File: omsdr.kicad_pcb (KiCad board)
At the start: 2 copper layers, 50 x 50 mm, 57 parts, among them J1 I/Q Out, J2 ANT, J3 ISP, J4 LO, J5 I/Q Out, J8 PWR, SW1 SW_SPST, SW2 SW_SPST, T1 CX2074NL, U1 LT6231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

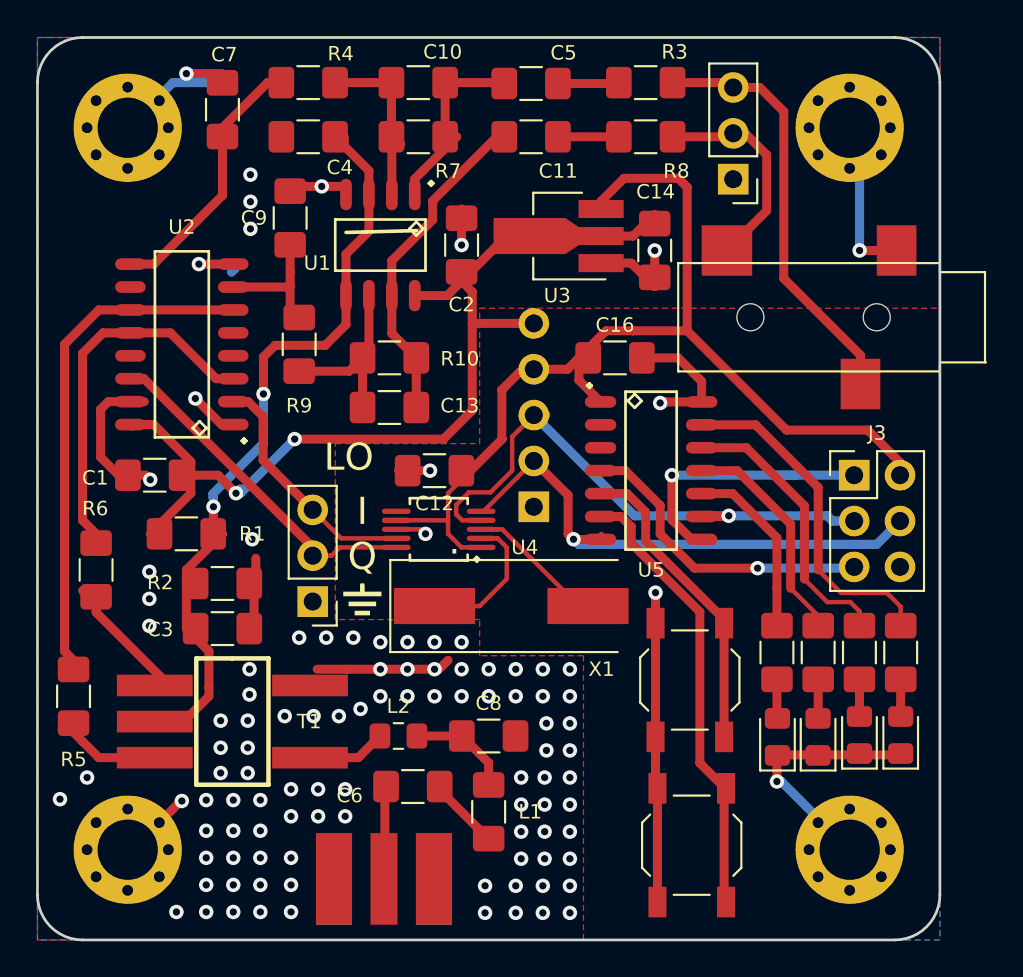
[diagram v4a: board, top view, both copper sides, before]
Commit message: Replaced connector footprints with versions from new kicad footprint library
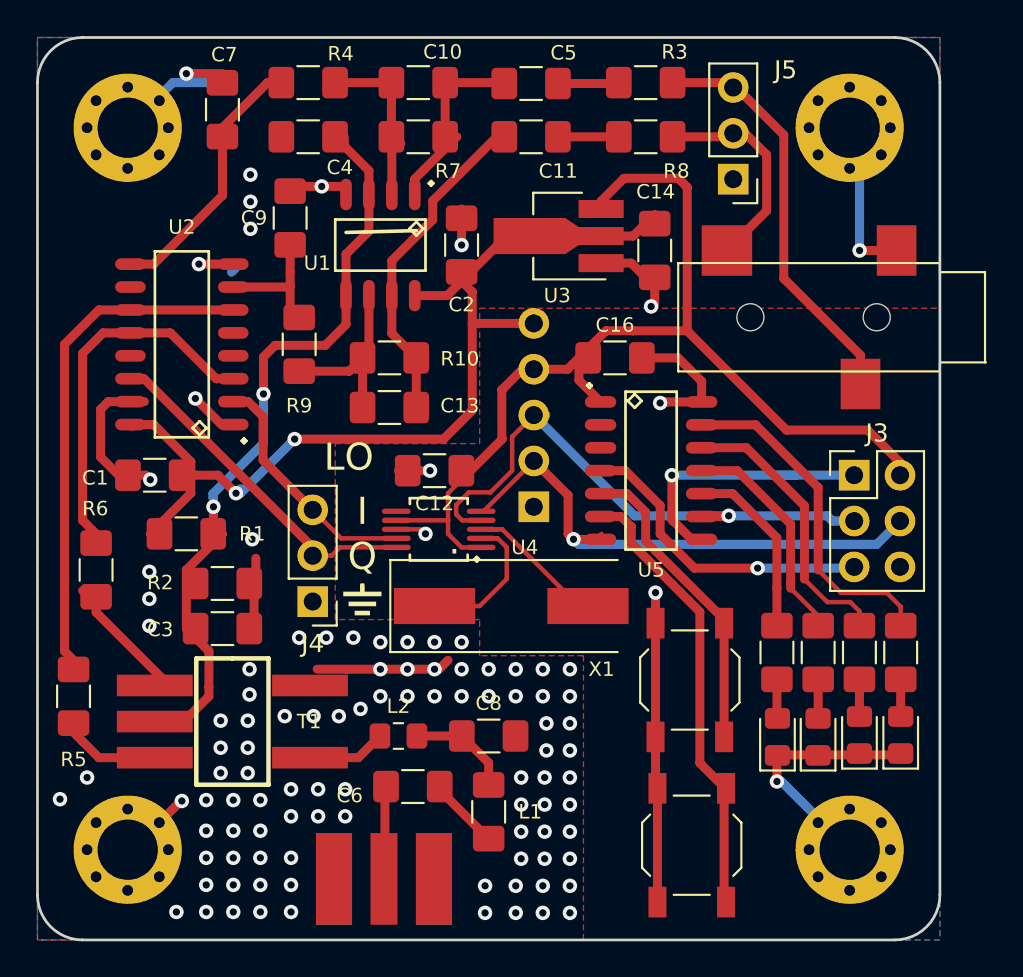
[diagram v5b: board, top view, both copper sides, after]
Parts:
- J3: footprint Pin_Headers:Pin_Header_Straight_2x03_Pitch2.54mm -> Connector_PinHeader_2.54mm:PinHeader_2x03_P2.54mm_Vertical
- J4: footprint Pin_Headers:Pin_Header_Straight_1x03_Pitch2.54mm -> Connector_PinHeader_2.54mm:PinHeader_1x03_P2.54mm_Vertical
- J8: footprint Pin_Headers:Pin_Header_Angled_1x05_Pitch2.54mm -> Connector_PinHeader_2.54mm:PinHeader_1x05_P2.54mm_Horizontal
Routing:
- net Net-(J1-Pad2): track 24.2 -> 23.4 mm

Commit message: Bumping version to 1.2 on schematic and PCB
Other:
- board text added: "OMSDR Rev. 1.2"
- board text removed: "OMSDR Rev. 1.1"
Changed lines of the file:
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@@
     (effects (font (size 1 1) (thickness 0.2)) (justify left mirror))
   )
-  (gr_text "OMSDR Rev. 1.1" (at 147.5 81.75) (layer B.SilkS)
+  (gr_text "OMSDR Rev. 1.2" (at 147.5 81.75) (layer B.SilkS)
     (effects (font (size 1.5 1.5) (thickness 0.3)) (justify left mirror))
   )

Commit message: Now official HB9UF project, add logo and rework silk.
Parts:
- added G***: LOGO, local:hb9uf_logo_small, B.Cu at (126.0, 88.0)
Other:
- board text added: "Based on work by T. Parks (c) 2017,18,19 CC-BY-SA"
- board text added: "HB9UF OMSDR"
- board text added: "by Matt Weyland HB9FRV, Rev. 1.2"
- board text removed: "Based on work by Tony Parks (c) 2017,18,19 CC-BY-SA"
- board text removed: "OMSDR Rev. 1.2"
- board text removed: "by Matt Weyland (HB9FRV) and Peter Klaentschi (HB9GHY)"

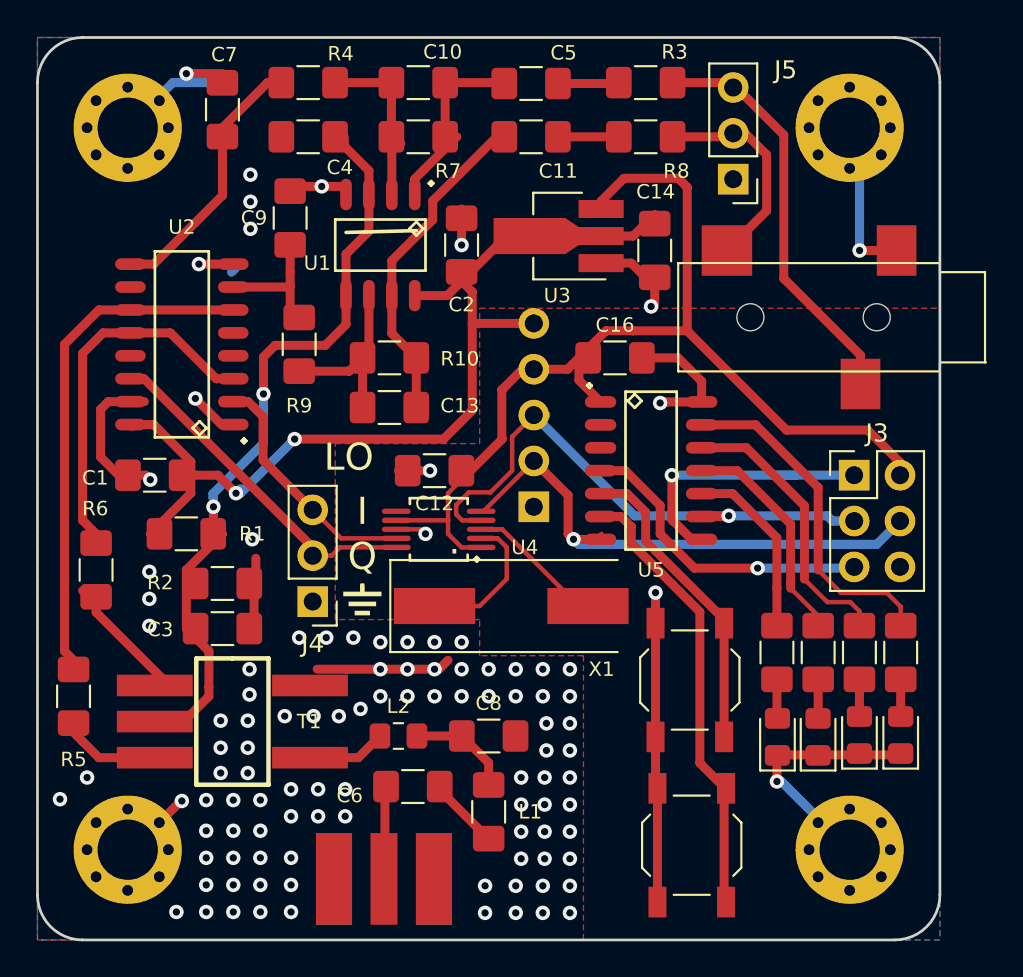
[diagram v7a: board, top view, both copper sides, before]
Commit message: Bumping to KiCad version 6.0
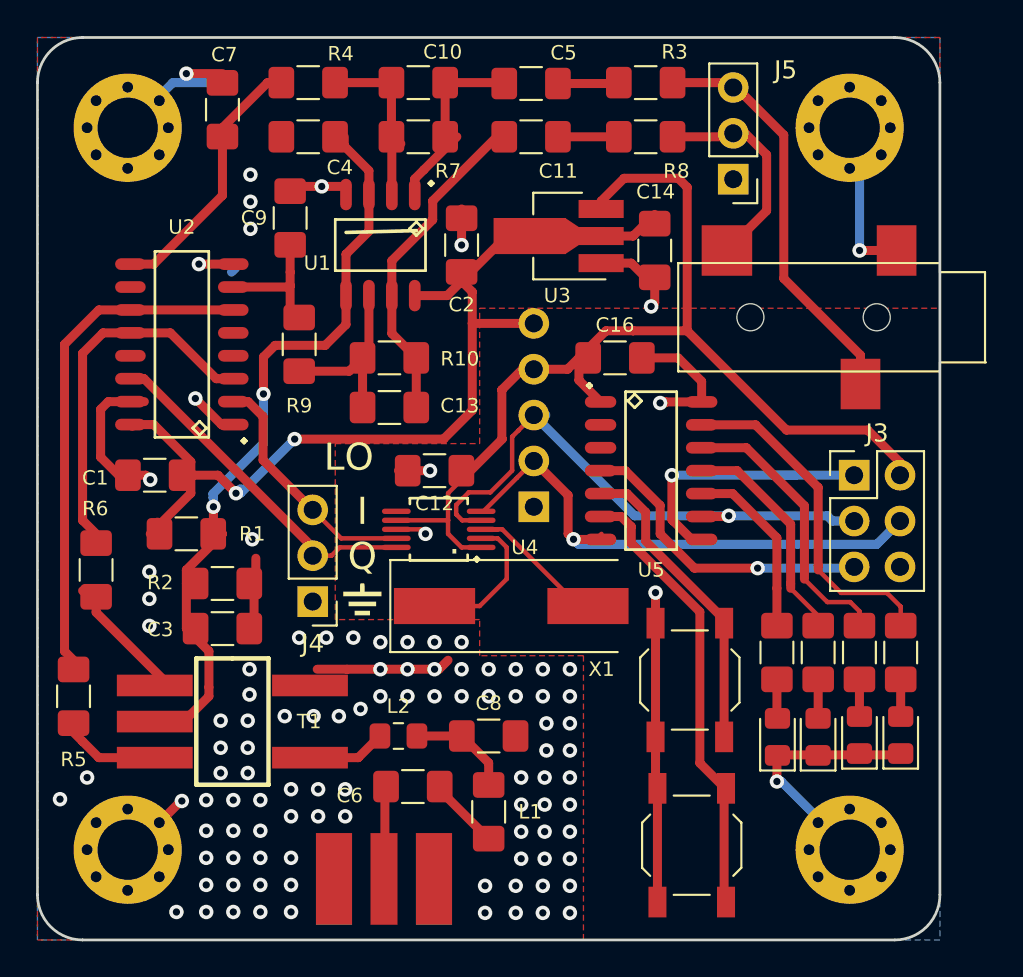
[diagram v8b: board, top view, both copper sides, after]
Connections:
- net /~RST renamed /~{RST}
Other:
- net class Default removed
